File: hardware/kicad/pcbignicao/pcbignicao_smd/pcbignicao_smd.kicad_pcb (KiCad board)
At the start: 2 copper layers, 85 x 70 mm, 36 parts, among them J10 ARM, J11 OLED, J12 EXP, J13 SAIDA_IGNICAO, J3 +buzzer, J4 -buzzer, J5 NO, J6 COM, J7 EXT_PWR, J8 RELE, J9 LED_BTN, U1 Ra-02, U2 PC817, U3 PC817

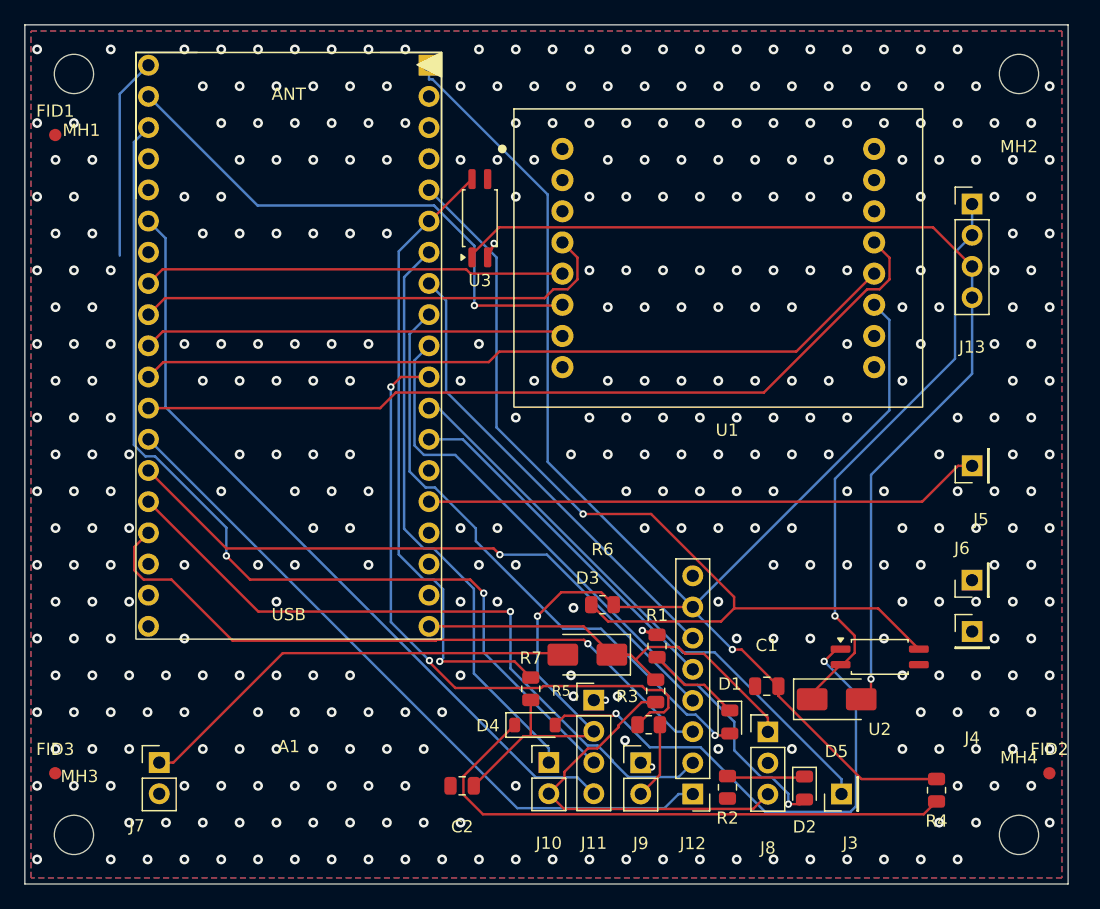
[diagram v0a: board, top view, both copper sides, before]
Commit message: feat(pcb): reduz vias de costura da ignição SMD (rev 2.1)
- Vias GND: 388 -> 101 (total 406 -> 119), espaçamento ~6-8 mm
- 2 vias de ponte amarram as ilhas de cobre perto de J9/J11
- DRC: 0 itens desconectados (antes 1, o ilhado documentado no README)
- Corrige título do PCB e sobe rev/data; gerbers e pacote JLCPCB regenerados
- Netlist revalidado: idêntico antes/depois
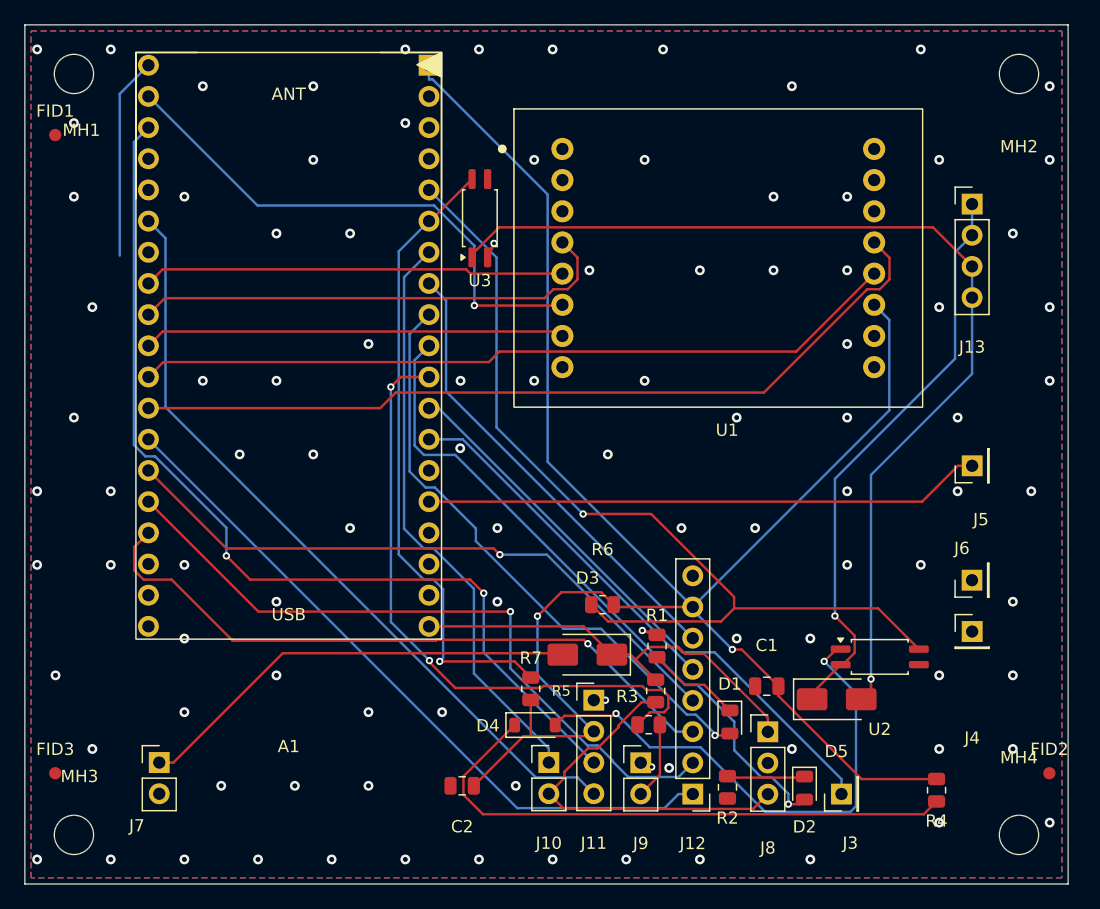
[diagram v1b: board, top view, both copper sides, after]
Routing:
- net GND: vias 388 -> 101
